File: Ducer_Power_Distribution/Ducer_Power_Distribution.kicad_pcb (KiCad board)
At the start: 2 copper layers, 115 x 67 mm, 16 parts, among them J1 Mini_Fit_Jr_1x3_pin, J10 Conn_01x05, J11 Power In, J2 Mini_Fit_Jr_1x3_pin, J3 Mini_Fit_Jr_1x3_pin, J4 Mini_Fit_Jr_1x3_pin, J5 Mini_Fit_Jr_1x3_pin, J6 Mini_Fit_Jr_1x3_pin, J7 Mini_Fit_Jr_1x3_pin, J8 Mini_Fit_Jr_1x3_pin, J9 Conn_01x05

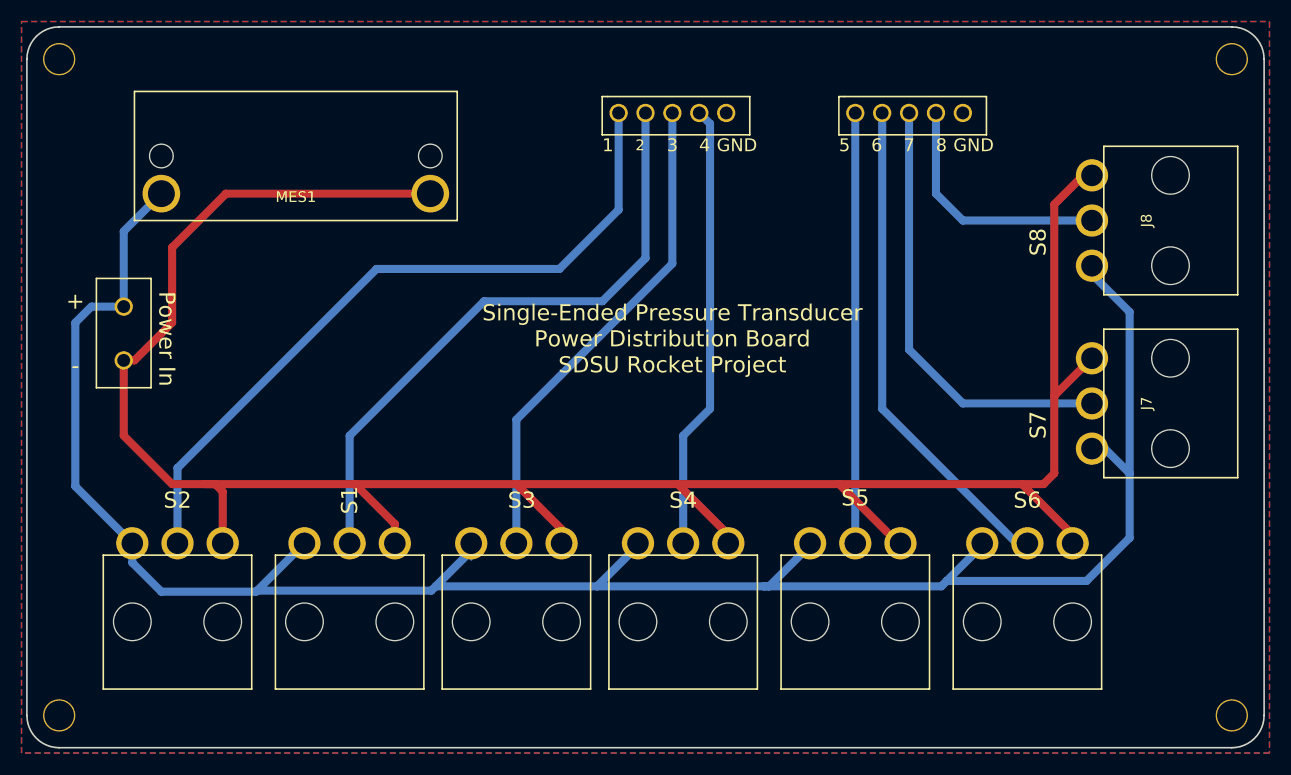
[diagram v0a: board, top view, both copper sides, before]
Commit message: Added aux port, mirrored layers
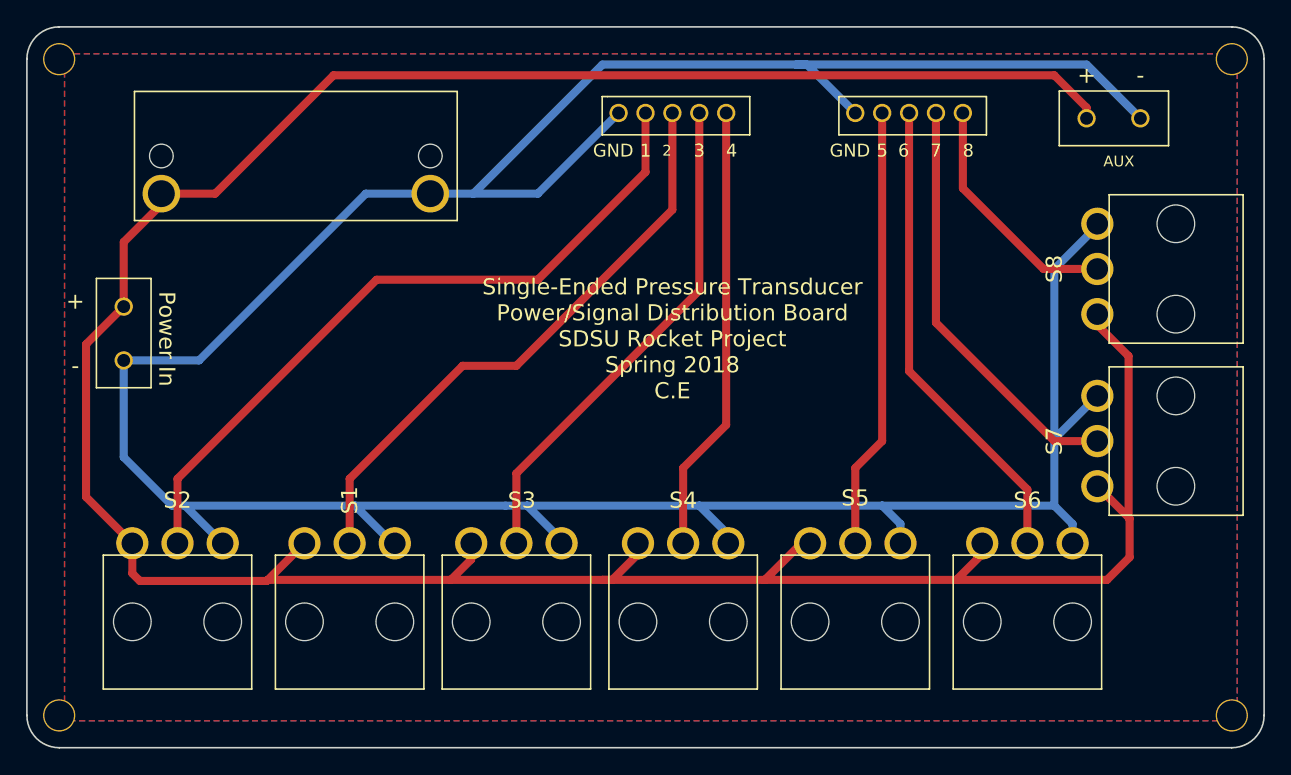
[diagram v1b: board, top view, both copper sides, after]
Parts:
- added AUX: Conn_01x02, mylibrary:01x02_5mm_Screw_Terminals, F.Cu at (148.0, 73.0)
- moved J8 4.53 mm to (149.0, 87.0)
- moved J7 3.54 mm to (149.0, 103.0)
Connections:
- J10 pad 1: Net-(J10-Pad1) -> GND
- J10 pad 5: GND -> Net-(J10-Pad5)
- J5 pad 2: Net-(J10-Pad1) -> Net-(J10-Pad2)
- J6 pad 2: Net-(J10-Pad2) -> Net-(J10-Pad3)
- J7 pad 2: Net-(J10-Pad3) -> Net-(J10-Pad4)
- J8 pad 2: Net-(J10-Pad4) -> Net-(J10-Pad5)
- J9 pad 1: Net-(J1-Pad2) -> GND
- J9 pad 2: Net-(J2-Pad2) -> Net-(J1-Pad2)
- J9 pad 3: Net-(J3-Pad2) -> Net-(J2-Pad2)
- J9 pad 4: Net-(J4-Pad2) -> Net-(J3-Pad2)
- J9 pad 5: GND -> Net-(J4-Pad2)
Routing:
- net VCC: track 204.0 -> 286.0 mm
- net GND: track 214.6 -> 291.2 mm
- net Net-(J10-Pad1): track 40.0 -> 0.00 mm
- net Net-(J10-Pad5): track 0.00 -> 24.8 mm
- net Net-(J10-Pad4): track 23.0 -> 40.5 mm
- net Net-(J10-Pad3): track 41.1 -> 46.6 mm
- net Net-(J10-Pad2): track 46.9 -> 41.7 mm
- net Net-(J2-Pad2): track 58.8 -> 56.4 mm
- net Net-(J3-Pad2): track 46.0 -> 47.7 mm
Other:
- board text added: "Single-Ended Pressure Transducer Power/Signal Distribution Board SDSU Rocket Project Spring 2018 C.E"
- board text removed: "Single-Ended Pressure Transducer Power Distribution Board SDSU Rocket Project"

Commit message: pre-purging AvTop
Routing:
- net VCC: track 286.0 -> 219.1 mm
- net GND: track 291.2 -> 257.7 mm
- net Net-(J10-Pad5): track 24.8 -> 27.1 mm
- net Net-(J2-Pad2): track 56.4 -> 55.2 mm
- net Net-(J10-Pad4): track 40.5 -> 41.0 mm
- net Net-(J1-Pad2): track 66.8 -> 67.4 mm
